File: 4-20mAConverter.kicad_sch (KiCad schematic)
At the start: 26 parts, among them J11 HT3.96mm-3P, Q17 NPN, U15 LM324, U16 LM317_TO-252, U17 TL431

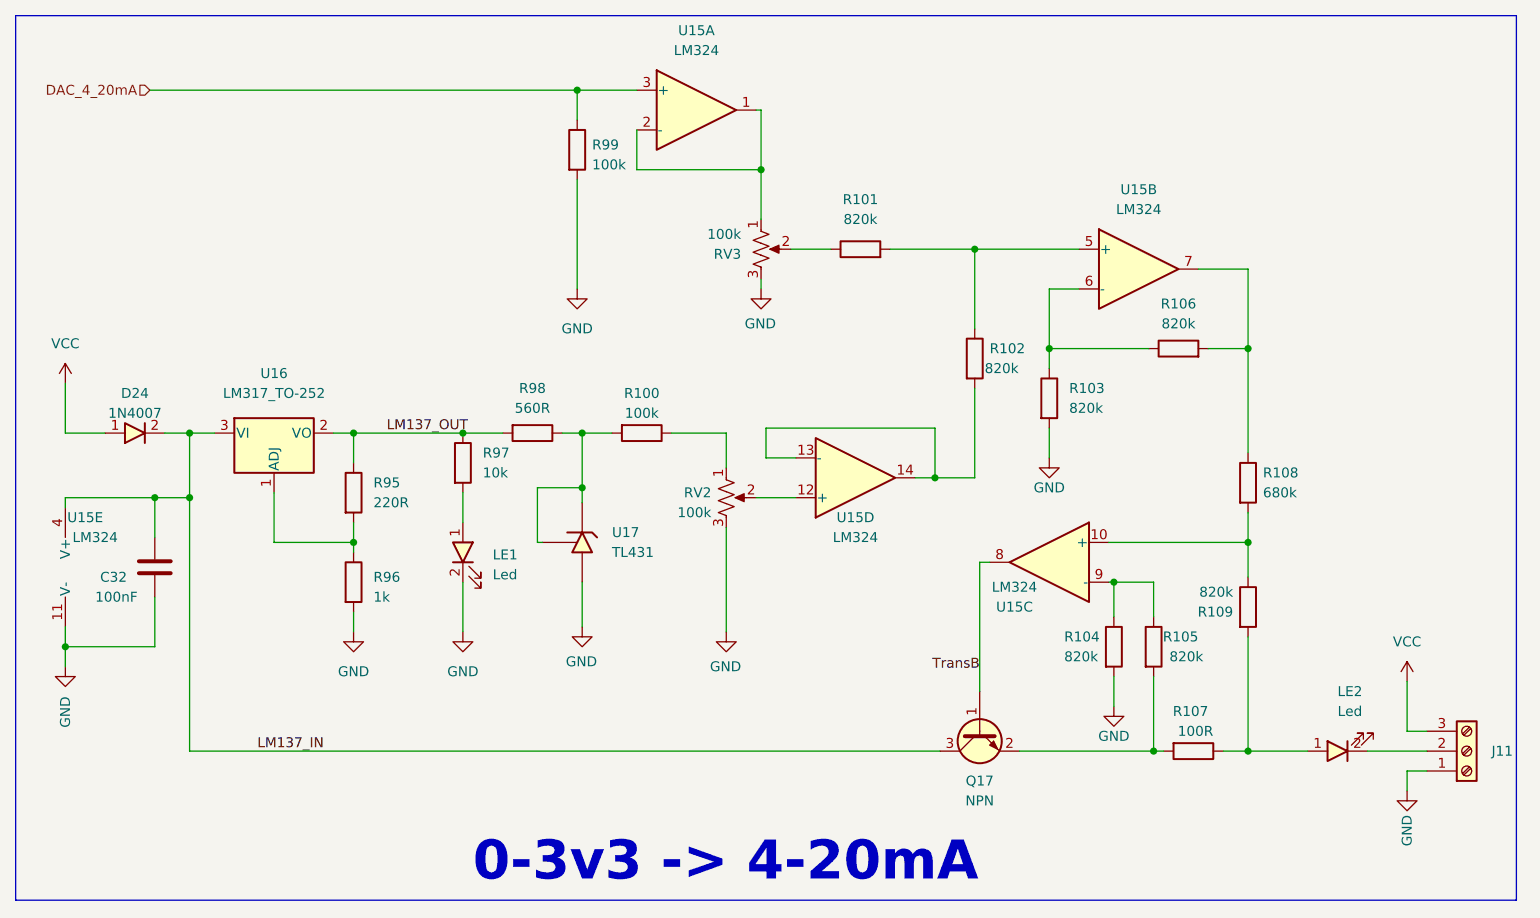
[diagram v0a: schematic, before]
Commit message: Add LORA, SDcard and Volt to 4_20mA scheamtic
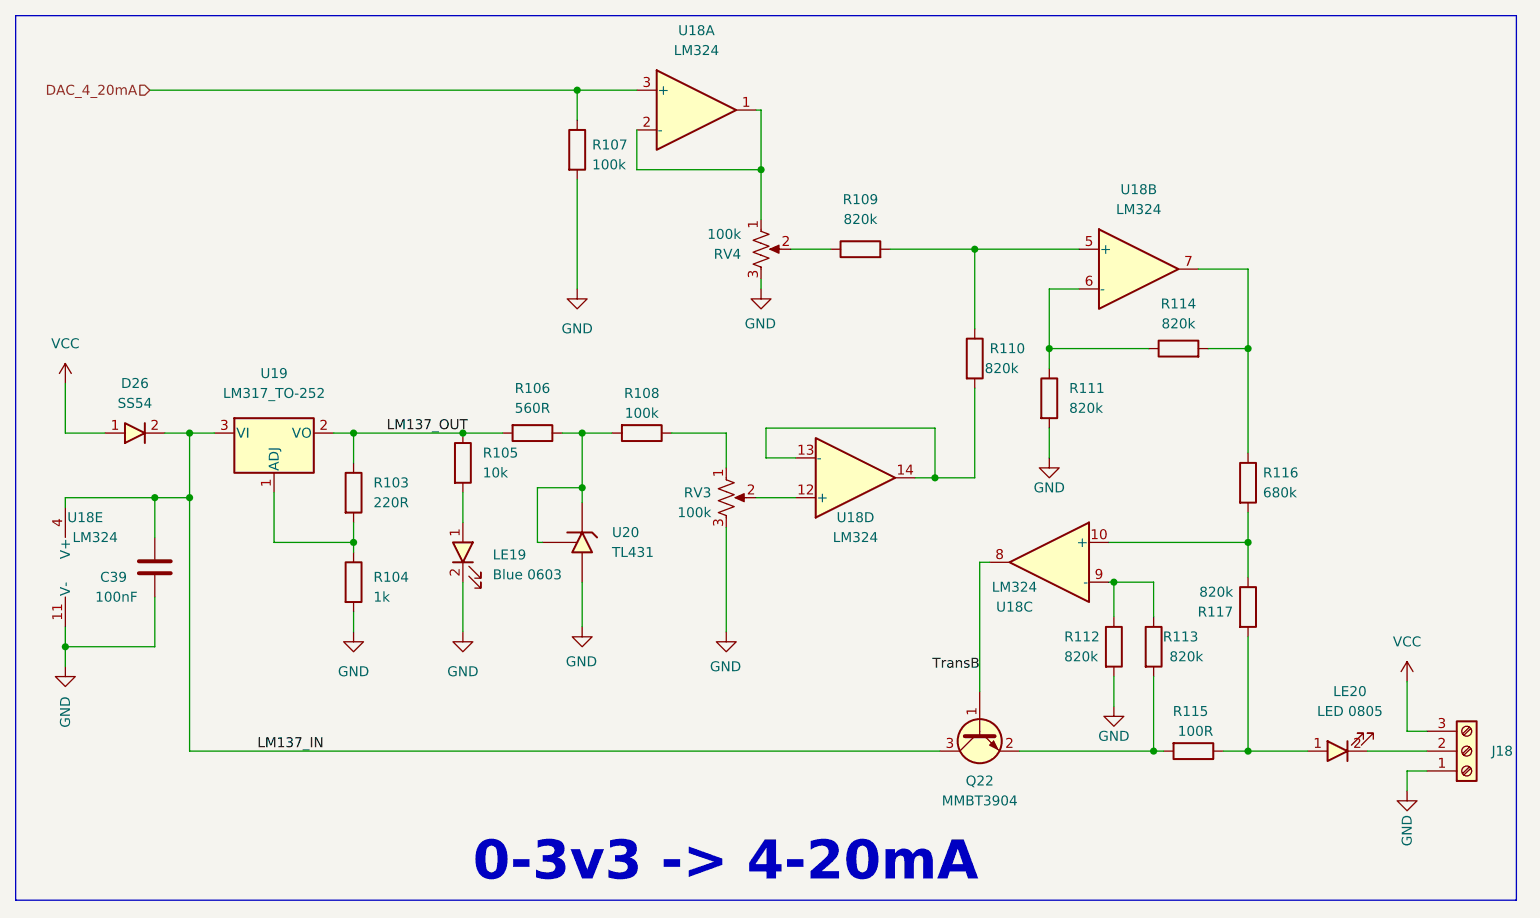
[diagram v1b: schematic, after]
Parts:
- C39: renamed from C32; footprint IVS_FOOTPRINTS:C0603 -> SpiritBoi_Footprint_Library:C_0603
- D26: renamed from D24; value 1N4007 -> SS54; footprint IVS_FOOTPRINTS:D_SMA -> SpiritBoi_Footprint_Library:Package-Diode-D_SMA
- J18: renamed from J11; footprint IVS_FOOTPRINTS:Terminal_HT-P3.96mm-3P-Vertical-Pluggable -> SpiritBoi_Footprint_Library:TerminalBlock_bornier-3_P5.08mm
- LE19: renamed from LE1; value Led -> Blue 0603; footprint IVS_FOOTPRINTS:LED0603 -> SpiritBoi_Footprint_Library:LED_0603
- LE20: renamed from LE2; value Led -> LED 0805; footprint IVS_FOOTPRINTS:LED0805 -> SpiritBoi_Footprint_Library:LED_0805
- Q22: renamed from Q17; value NPN -> MMBT3904; footprint IVS_FOOTPRINTS:SOT23-3 -> SpiritBoi_Footprint_Library:SOT23-3
- R103: renamed from R95; footprint IVS_FOOTPRINTS:R0603 -> SpiritBoi_Footprint_Library:R_0603
- R104: renamed from R96; footprint IVS_FOOTPRINTS:R0603 -> SpiritBoi_Footprint_Library:R_0603
- R105: renamed from R97; footprint IVS_FOOTPRINTS:R0603 -> SpiritBoi_Footprint_Library:R_0603
- R106: renamed from R98; footprint IVS_FOOTPRINTS:R0603 -> SpiritBoi_Footprint_Library:R_0603
- R107: renamed from R99; footprint IVS_FOOTPRINTS:R0603 -> SpiritBoi_Footprint_Library:R_0603
- R108: renamed from R100; footprint IVS_FOOTPRINTS:R0603 -> SpiritBoi_Footprint_Library:R_0603
- R109: renamed from R101; footprint IVS_FOOTPRINTS:R0603 -> SpiritBoi_Footprint_Library:R_0603
- R110: renamed from R102; footprint IVS_FOOTPRINTS:R0603 -> SpiritBoi_Footprint_Library:R_0603
- R111: renamed from R103; footprint IVS_FOOTPRINTS:R0603 -> SpiritBoi_Footprint_Library:R_0603
- R112: renamed from R104; footprint IVS_FOOTPRINTS:R0603 -> SpiritBoi_Footprint_Library:R_0603
- R113: renamed from R105; footprint IVS_FOOTPRINTS:R0603 -> SpiritBoi_Footprint_Library:R_0603
- R114: renamed from R106; footprint IVS_FOOTPRINTS:R0603 -> SpiritBoi_Footprint_Library:R_0603
- R115: renamed from R107; footprint IVS_FOOTPRINTS:R0603 -> SpiritBoi_Footprint_Library:R_0603
- R116: renamed from R108; footprint IVS_FOOTPRINTS:R0603 -> SpiritBoi_Footprint_Library:R_0603
- R117: renamed from R109; footprint IVS_FOOTPRINTS:R0603 -> SpiritBoi_Footprint_Library:R_0603
- RV3: renamed from RV2; footprint IVS_FOOTPRINTS:Potentiometer_Bourns_TC33X_Vertical -> SpiritBoi_Footprint_Library:Potentiometer-Vert-THT-Bourns_3296W
- RV4: renamed from RV3; footprint IVS_FOOTPRINTS:Potentiometer_Bourns_TC33X_Vertical -> SpiritBoi_Footprint_Library:Potentiometer-Vert-THT-Bourns_3296W
- U18: renamed from U15; footprint IVS_FOOTPRINTS:SOIC14 -> SpiritBoi_Footprint_Library:Package-IC-Vert-SMD-1.27mm-14P-SOIC_14_Narrow_3.9x8.7mm
- U19: renamed from U16; footprint Package_TO_SOT_SMD:TO-252-2 -> SpiritBoi_Footprint_Library:Package-IC-Vert-SMD-TO_252_2
- U20: renamed from U17; footprint IVS_FOOTPRINTS:SOT23-3 -> SpiritBoi_Footprint_Library:SOT23-3
